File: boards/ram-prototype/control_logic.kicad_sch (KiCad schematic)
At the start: 18 parts, among them U1 74LVC1G04, U2 74LVC1G04, U3 74LVC1G04, U4 74LVC1G08, U5 74LVC1G08, U6 74LVC1G08

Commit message: Partway through erc debugging
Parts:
- removed D1, D2, D3, D4, D5, D6: Red, symbol LED_Small
- removed R1, R2, R3, R4, R5, R6: 680R, symbol R_Small
- removed U1, U2, U3: 74LVC1G04, symbol 74LVC1G04
- removed U4, U5, U6: 74LVC1G08, symbol 74LVC1G08
- added D1, D2, D3, D4, D5, D6: Red, symbol Device:LED_Small
- added R1, R2, R3, R4, R5, R6: 680R, symbol Device:R_Small
- added U1, U2, U3: 74LVC1G04, symbol 74xGxx:74LVC1G04
- added U4, U5, U6: 74LVC1G08, symbol 74xGxx:74LVC1G08
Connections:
- net CE: now also R1.1, U1.4, U4.1, U5.1
- net CE_AND_OE: now also R5.1, U5.4, U6.1
- net GND: now also D1.1 (K), D2.1 (K), D3.1 (K), D4.1 (K), D5.1 (K), D6.1 (K), U1.3 (GND), U2.3 (GND), U3.3 (GND), U4.3 (GND), U5.3 (GND), U6.3 (GND)
- net OE: now also R2.1, U2.4, U5.2
- net READ_EN: now also R6.1, U6.4
- net VCC: now also U1.5 (VCC), U2.5 (VCC), U3.5 (VCC), U4.5 (VCC), U5.5 (VCC), U6.5 (VCC)
- net WE: now also R3.1, U3.4, U4.2
- net WRITE_ACTIVE: now also R4.1, U4.4
- net nCE: now also U1.2
- net nOE: now also U2.2
- net nWE: now also U3.2, U6.2
- new net: D1.2 (A), R1.2
- new net: D4.2 (A), R4.2
- new net: D5.2 (A), R5.2
- new net: D3.2 (A), R3.2
- new net: D6.2 (A), R6.2
- new net: D2.2 (A), R2.2

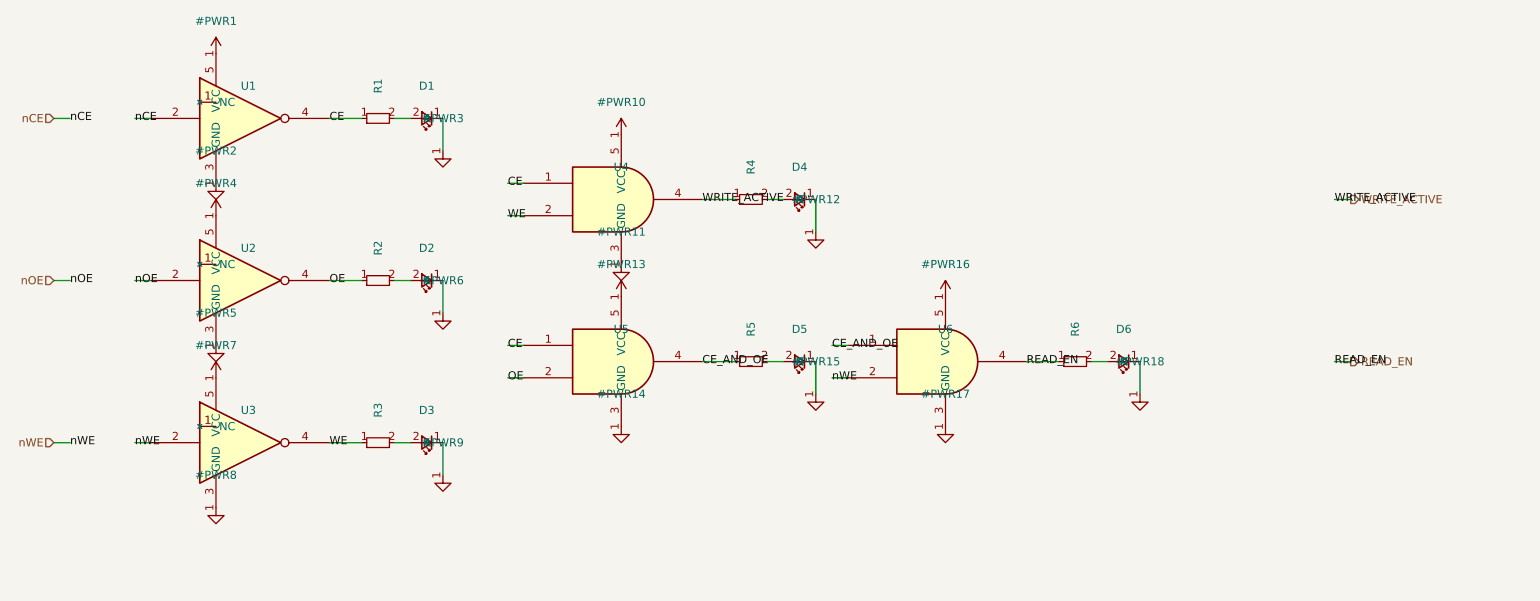
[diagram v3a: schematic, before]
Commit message: Start cleaning up the schematic
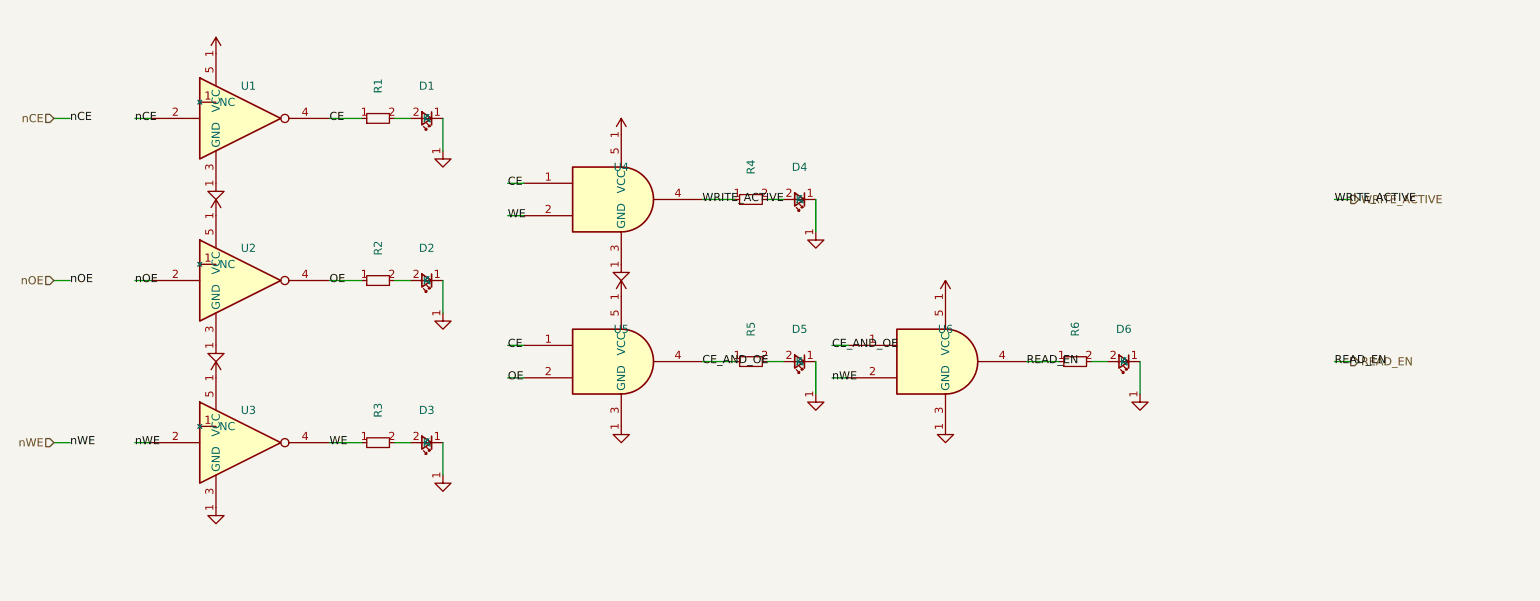
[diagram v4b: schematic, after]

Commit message: Schematic is starting to look good
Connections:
- net CE is gone; now on an unnamed net: R1.1, U1.4, U4.1, U5.1
- net WE is gone; now on an unnamed net: R3.1, U3.4, U4.2
- net WRITE_ACTIVE: now also R5.1; no longer R4.1
- net at D1.2 (A), R1.2: now also D2.2 (A), R2.2
- net CE_AND_OE: no longer names the net of U5.4, U6.1
- net CE_AND_OE: now also R4.1; no longer R5.1
- net OE: no longer names the net of R2.1, U2.4, U5.2

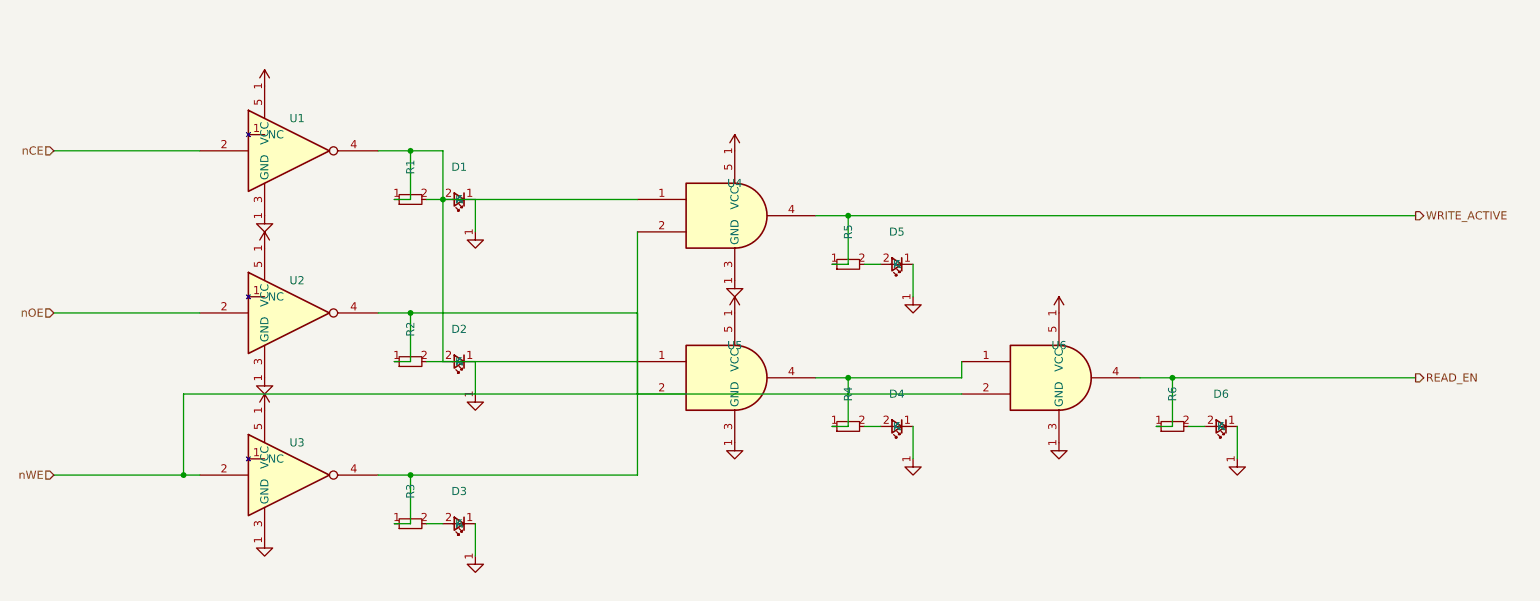
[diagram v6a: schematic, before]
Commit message: Create verification script
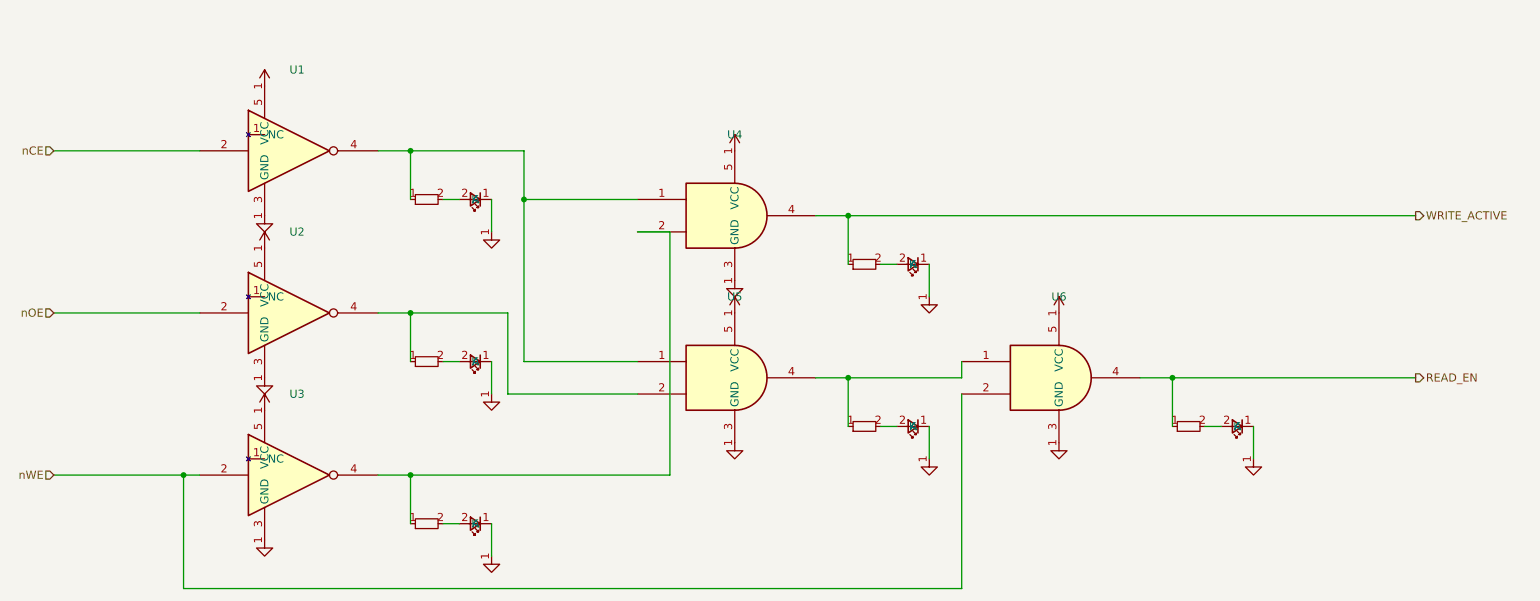
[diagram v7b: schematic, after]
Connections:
- net at R1.1, U1.4, U4.1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: no longer D1.2 (A), D2.2 (A), R1.2, R2.2
- net at R3.1, U3.4, U4.2: no longer R2.1, U2.4, U5.2
- new net: R2.1, U2.4, U5.2
- new net: D2.2 (A), R2.2
- new net: D1.2 (A), R1.2
